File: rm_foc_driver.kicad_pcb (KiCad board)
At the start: 4 copper layers, 70 x 70 mm, 70 parts, among them J1 SWD, J3 UART, J4 TMC4671, J5 Conn_01x07, J6 Conn_01x02, J8 Conn_01x03, Q1 CSD18540Q5B, Q2 CSD18540Q5B, Q3 CSD18540Q5B, Q4 CSD18540Q5B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

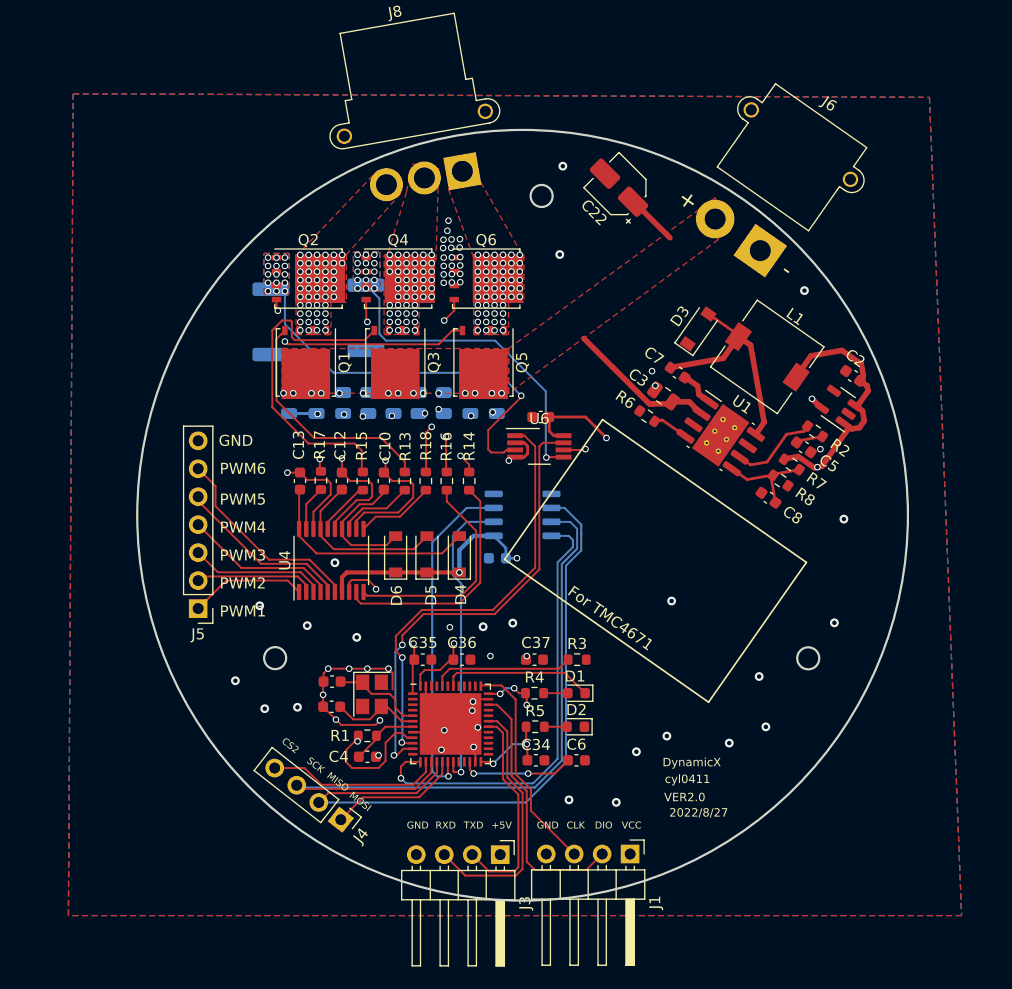
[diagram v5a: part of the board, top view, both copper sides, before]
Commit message: ir2104 version
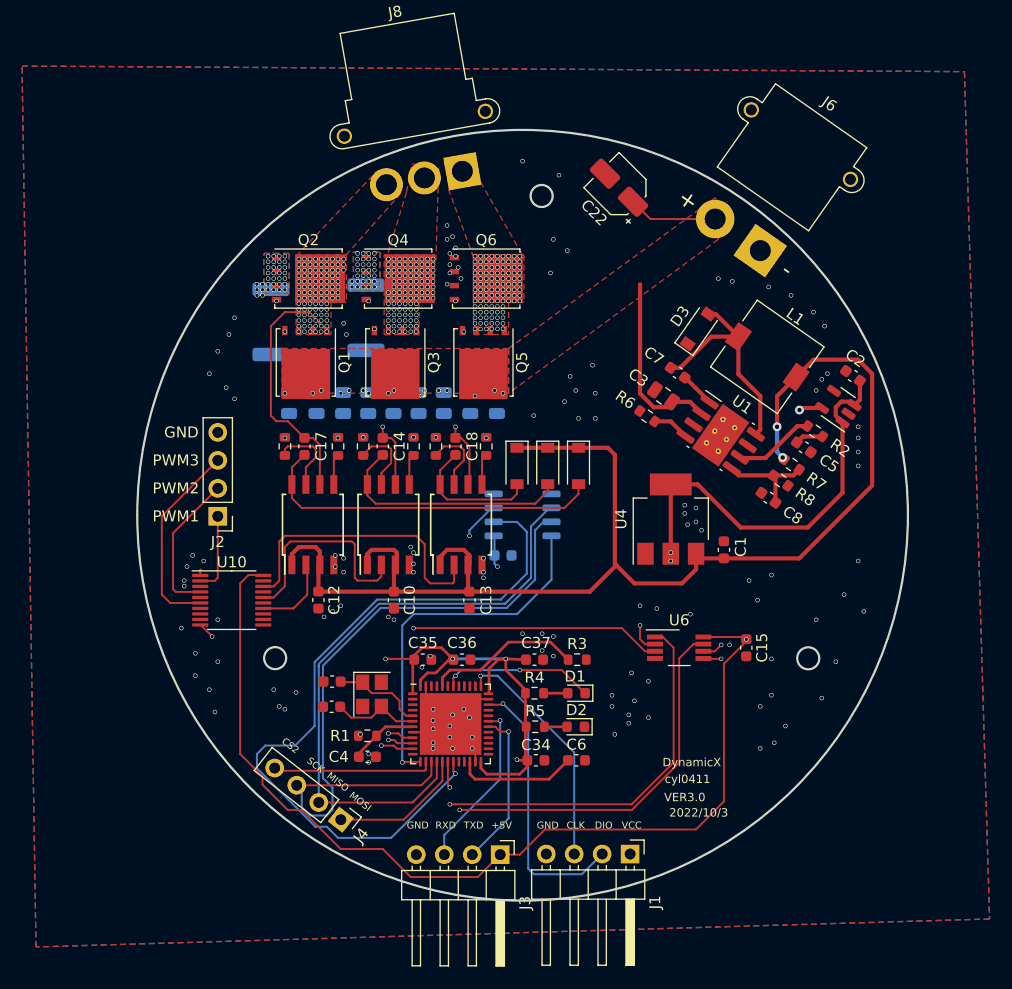
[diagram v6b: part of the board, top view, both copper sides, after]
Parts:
- removed J5: Conn_01x07, Connector_PinHeader_2.54mm:PinHeader_1x07_P2.54mm_Vertical
- removed R17, R18: 10R, Resistor_SMD:R_0603_1608Metric
- added C1: 1uF, Capacitor_SMD:C_0603_1608Metric, F.Cu at (183.4, 104.1)
- added C14: 100nF, Capacitor_SMD:C_0603_1608Metric, F.Cu at (152.4, 94.7)
- added C17: 100nF, Capacitor_SMD:C_0603_1608Metric, F.Cu at (145.3, 94.7)
- added C18: 100nF, Capacitor_SMD:C_0603_1608Metric, F.Cu at (159.0, 94.7)
- added J2: TMC4671, Connector_PinHeader_2.54mm:PinHeader_1x04_P2.54mm_Vertical, F.Cu at (137.4, 101.1)
- added R12: 20R, Resistor_SMD:R_0603_1608Metric, F.Cu at (155.2, 94.7)
- added R9: 20R, Resistor_SMD:R_0603_1608Metric, F.Cu at (150.6, 94.7)
- added U10: 74HC244, Package_SO:TSSOP-20_4.4x5mm_P0.5mm, F.Cu at (138.7, 108.7)
- added U5: IR2104, Package_SO:SOIC-8W_5.3x5.3mm_P1.27mm, F.Cu at (152.9, 101.9)
- added U8: IR2104, Package_SO:SOIC-8W_5.3x5.3mm_P1.27mm, F.Cu at (146.1, 101.9)
- added U9: IR2104, Package_SO:SOIC-8W_5.3x5.3mm_P1.27mm, F.Cu at (159.5, 101.9)
- R13, R14, R15, R16: value 10R -> 20R
- R7: value 105k -> 210k
- R8: value 20k -> 15k
- U4: value EG2133 -> AMS1117-5.0; footprint Package_SO:TSSOP-20_4.4x6.5mm_P0.65mm -> Package_TO_SOT_SMD:SOT-223-3_TabPin2
- moved U4 31.1 mm to (178.6, 101.3)
- moved C15 28.1 mm to (185.4, 113.0), turned to -90 degrees
- moved U6 22.3 mm to (179.3, 113.0)
- moved C13 18.8 mm to (160.3, 108.7), turned to -90 degrees
- moved D5 15.9 mm to (170.2, 96.5), turned to -90 degrees
- moved D6 13.6 mm to (164.6, 96.5), turned to -90 degrees
- moved R14 12.3 mm to (148.3, 94.7), turned to -90 degrees
- moved D4 11.4 mm to (167.4, 96.5), turned to -90 degrees
- moved R13 11.3 mm to (143.5, 94.7), turned to -90 degrees
- moved C12 11.0 mm to (146.6, 108.7), turned to -90 degrees
- moved C10 10.9 mm to (153.4, 108.7), turned to -90 degrees
- moved R15 7.34 mm to (157.2, 94.7), turned to -90 degrees
- moved R16 4.77 mm to (161.8, 94.7), turned to -90 degrees
- moved C16 0.57 mm to (163.3, 104.6), turned to 0 degrees
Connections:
- C10 pad 1: Net-(C10-Pad1) -> +12V
- C10 pad 2: /SH_A -> GND
- C12 pad 1: Net-(C12-Pad1) -> +12V
- C12 pad 2: /SH_B -> GND
- C13 pad 1: Net-(C13-Pad1) -> +12V
- C13 pad 2: /SH_C -> GND
- C22 pad 1: +12V -> +24V
- C24 pad 1: +12V -> +24V
- C25 pad 1: +12V -> +24V
- C26 pad 1: +12V -> +24V
- C27 pad 1: +12V -> +24V
- C29 pad 1: +12V -> +24V
- C3 pad 1: +12V -> +24V
- C30 pad 1: +12V -> +24V
- C31 pad 1: +12V -> +24V
- C32 pad 1: +12V -> +24V
- C33 pad 1: +12V -> +24V
- D4 pad 1: +5V -> +12V
- D4 pad 2: Net-(C13-Pad1) -> Net-(C14-Pad1)
- D5 pad 1: +5V -> +12V
- D5 pad 2: Net-(C12-Pad1) -> Net-(C17-Pad1)
- D6 pad 1: +5V -> +12V
- D6 pad 2: Net-(C10-Pad1) -> Net-(C18-Pad1)
- J6 pad 2: +12V -> +24V
- L1 pad 2: +5V -> +12V
- Q1 pad 5: +12V -> +24V
- Q3 pad 5: +12V -> +24V
- Q5 pad 5: +12V -> +24V
- R13 pad 1: Net-(R13-Pad1) -> /GH_A
- R13 pad 2: /GH_A -> Net-(R13-Pad2)
- R14 pad 1: Net-(R14-Pad1) -> /GL_A
- R14 pad 2: /GL_A -> Net-(R14-Pad2)
- R15 pad 1: Net-(R15-Pad1) -> /GH_C
- R15 pad 2: /GH_B -> Net-(R15-Pad2)
- R16 pad 1: Net-(R16-Pad1) -> /GL_C
- R16 pad 2: /GL_B -> Net-(R16-Pad2)
- R7 pad 1: +5V -> +12V
- U1 pad 2: +12V -> +24V
- U4 pad 1: /PWM1 -> GND
- U4 pad 2: /PWM2 -> +5V
- U4 pad 3: /PWM3 -> +12V
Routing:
- net +12V: track 18.4 -> 125.0 mm, vias 15 -> 2
- net +3.3V: track 155.0 -> 114.8 mm, vias 10 -> 7
- net /MODE: track 27.6 -> 67.4 mm
- net Net-(C17-Pad1): track 0.00 -> 32.2 mm
- net /SL_A: track 35.9 -> 65.5 mm, vias 16 -> 35
- net /SH_B: track 42.4 -> 15.3 mm, vias 50 -> 107
- net /PWMA: track 0.00 -> 26.5 mm
- net /SL_B: track 29.8 -> 55.3 mm, vias 16 -> 31
- net /SH_C: track 40.8 -> 15.8 mm, vias 53 -> 112
- net +24V: track 0.00 -> 25.0 mm, vias 0 -> 16
- net Net-(C14-Pad1): track 0.00 -> 22.1 mm
- net GND: track 45.6 -> 23.6 mm, vias 72 -> 134
- net Net-(R14-Pad1): track 21.7 -> 0.00 mm
- net /GH_C: track 31.1 -> 10.7 mm
- net Net-(R16-Pad1): track 20.3 -> 0.00 mm
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- added copper zone on F.Cu, net +24V
- removed copper zone on F.Cu, net +12V
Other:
- board text added: "2022/10/3"
- board text added: "VER3.0"
- board text removed: "2022/8/27"
- board text removed: "For TMC4671"
- board text removed: "PWM4"
- board text removed: "PWM5"
- board text removed: "PWM6"
- board text removed: "VER2.0"

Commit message: correct some bug yesterday
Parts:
- moved C4 0.38 mm to (150.6, 122.9)
- moved R1 0.38 mm to (150.6, 121.0)
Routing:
- net +3.3V: track 114.8 -> 116.6 mm
- net /SL_A: track 65.5 -> 66.8 mm, vias 35 -> 16
- net Net-(C4-Pad1): track 6.21 -> 6.75 mm
- net /SL_B: track 55.3 -> 55.2 mm, vias 31 -> 16
- net GND: vias 134 -> 129
- net /SH_C: vias 112 -> 37
- net /SH_B: vias 107 -> 35
- net /SH_A: vias 103 -> 36
- net +24V: vias 16 -> 14
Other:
- board text added: "Q2"

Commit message: update package
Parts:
- U10: footprint Package_SO:TSSOP-20_4.4x5mm_P0.5mm -> Package_SO:TSSOP-20_4.4x6.5mm_P0.65mm
- U5, U8, U9: footprint Package_SO:SOIC-8W_5.3x5.3mm_P1.27mm -> Package_SO:SOP-8_3.9x4.9mm_P1.27mm
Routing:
- net +12V: track 125.0 -> 127.2 mm
- net GND: track 23.6 -> 21.5 mm
- net /PWMB: track 19.4 -> 21.3 mm
- net /PWMA: track 26.5 -> 28.3 mm
- net /PWMC: track 7.27 -> 8.39 mm
- net Net-(R13-Pad2): track 7.15 -> 8.18 mm
- net Net-(R9-Pad2): track 6.60 -> 7.63 mm
- net Net-(R16-Pad2): track 2.79 -> 3.82 mm
- net Net-(R14-Pad2): track 2.79 -> 3.82 mm
- net Net-(R12-Pad2): track 2.79 -> 3.82 mm
- net /SH_C: track 15.8 -> 16.8 mm
- net /SH_B: track 15.3 -> 16.3 mm
- net /SH_A: track 23.6 -> 24.6 mm
- net Net-(R15-Pad2): track 6.55 -> 7.58 mm
- net Net-(C14-Pad1): track 22.1 -> 22.9 mm
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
